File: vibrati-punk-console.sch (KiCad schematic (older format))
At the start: 22 parts, among them J1 Conn_01x02_Male, J2 Conn_01x02_Male, U1 NE555, U2 NE555, U3 NE555

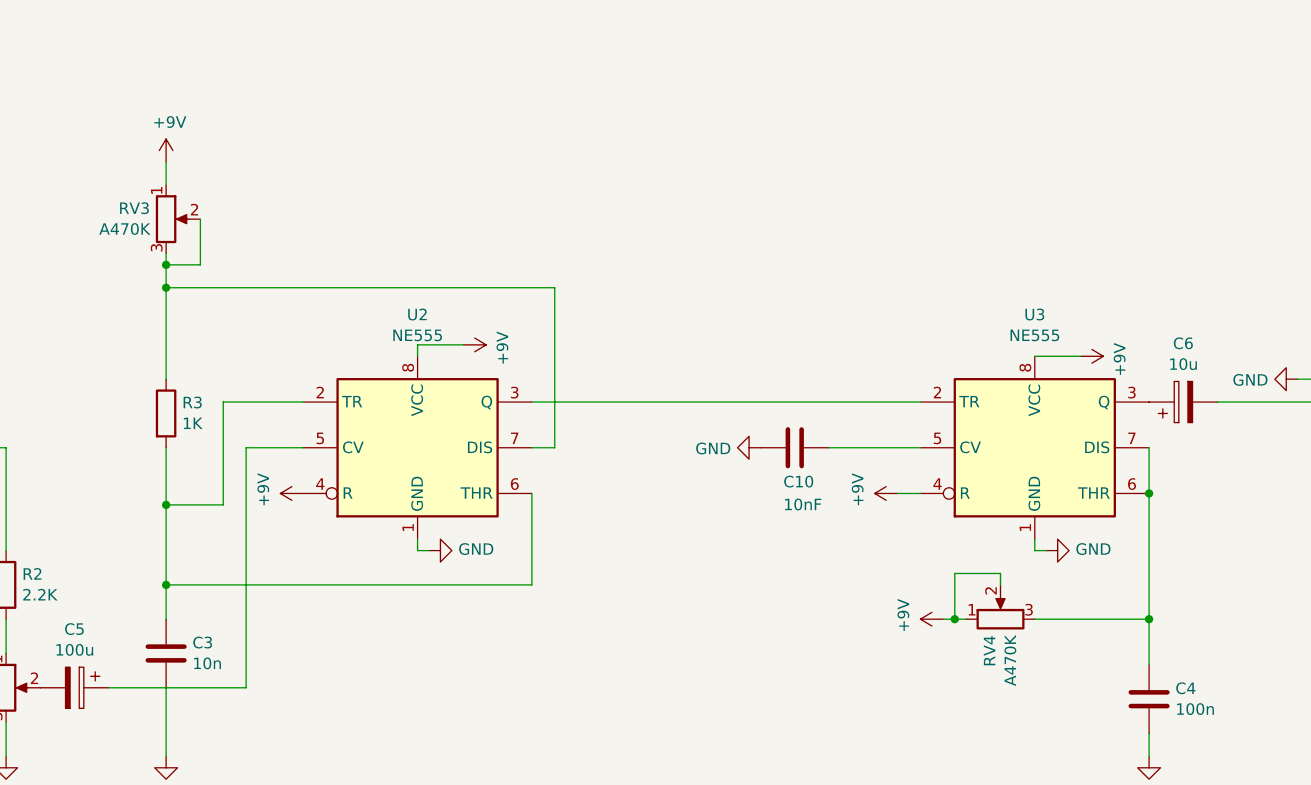
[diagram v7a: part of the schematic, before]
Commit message: Invert potentiometers for better results
The frequency should go up with the knob
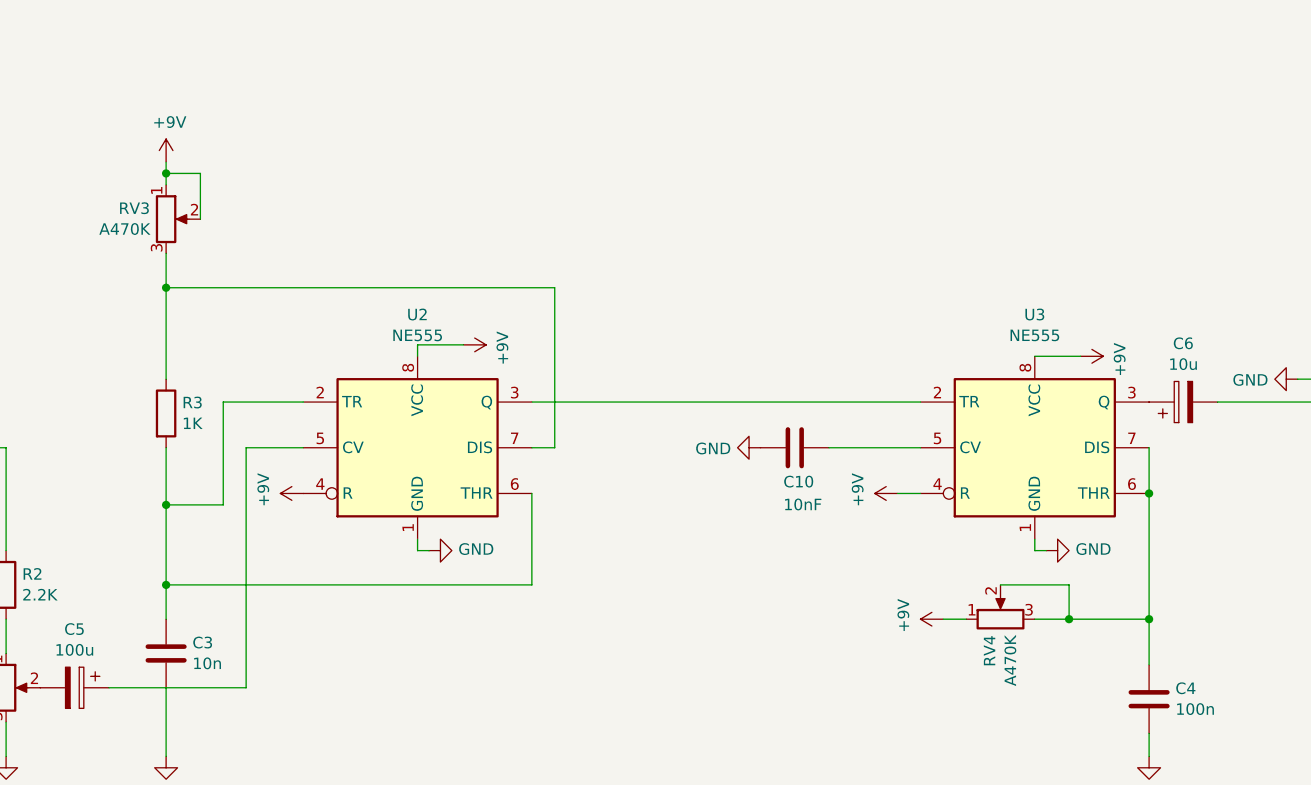
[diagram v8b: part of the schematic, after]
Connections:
- net +9V: now also RV3.2; no longer RV4.2
- net at R3.1, RV3.3, U2.7 (DIS): no longer RV3.2
- net at C4.1, RV4.3, U3.6 (THR)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: now also RV4.2
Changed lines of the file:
@@
 	10700 1750 10150 1750
 Wire Wire Line
-	4350 1950 4350 2050
+	4350 1950 4350 2000
 Wire Wire Line
 	3650 4550 3650 4400
@@
 Wire Wire Line
 	2200 3400 2350 3400
-Wire Wire Line
-	4350 2400 4350 2500
-Connection ~ 4350 2400
-Wire Wire Line
-	4500 2400 4350 2400
-Wire Wire Line
-	4500 2200 4500 2400
 Wire Wire Line
 	4350 2500 4350 2900
 Connection ~ 4350 2500
-Wire Wire Line
-	4350 2350 4350 2400
 Wire Wire Line
 	850  3000 850  3050
@@
 	8200 3650 8150 3650
 Wire Wire Line
-	8150 3950 8650 3950
+	8150 3950 8300 3950
 Connection ~ 8650 3950
-Wire Wire Line
-	7850 3950 7800 3950
-Connection ~ 7800 3950
-Wire Wire Line
-	7800 3950 7750 3950
 Wire Wire Line
 	8650 3950 8650 4150
@@
 Wire Wire Line
 	9300 2900 9400 2900
-Wire Wire Line
-	8000 3800 8000 3750
-Wire Wire Line
-	8000 3750 7800 3750
-Wire Wire Line
-	7800 3750 7800 3950
 $Comp
 L Device:C C10
@@
 	0    1    1    0
 $EndComp
+Wire Wire Line
+	7750 3950 7850 3950
+Wire Wire Line
+	4350 2350 4350 2500
+Wire Wire Line
+	8300 3800 8300 3950
+Wire Wire Line
+	8000 3800 8300 3800
+Connection ~ 8300 3950
+Wire Wire Line
+	8300 3950 8650 3950
+Wire Wire Line
+	4500 2200 4500 2000
+Wire Wire Line
+	4500 2000 4350 2000
+Connection ~ 4350 2000
+Wire Wire Line
+	4350 2000 4350 2050
 $EndSCHEMATC
